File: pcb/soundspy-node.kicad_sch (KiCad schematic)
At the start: 1 part

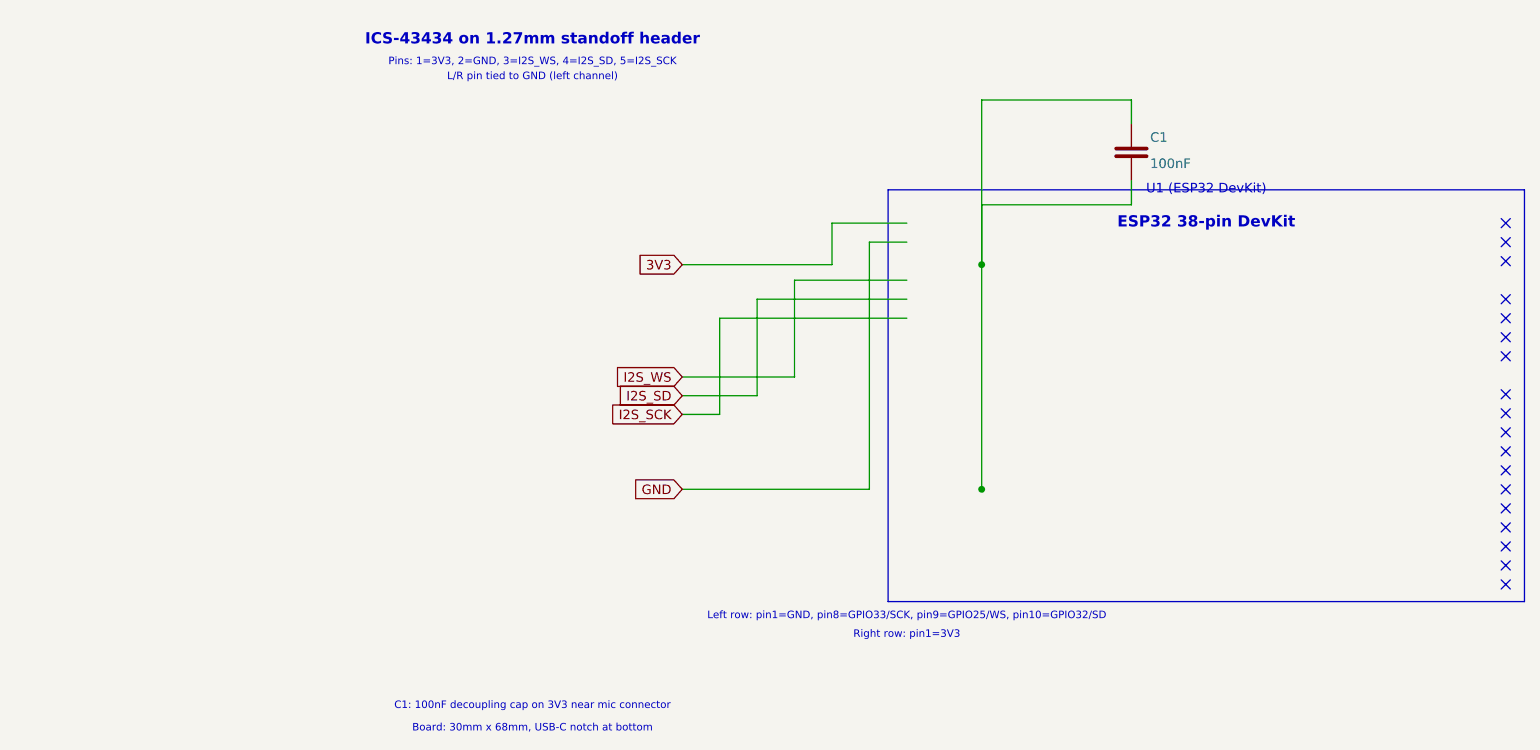
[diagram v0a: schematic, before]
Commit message: Fix PCB and schematic files: remove invalid ;; comments, simplify schematic to valid KiCad syntax
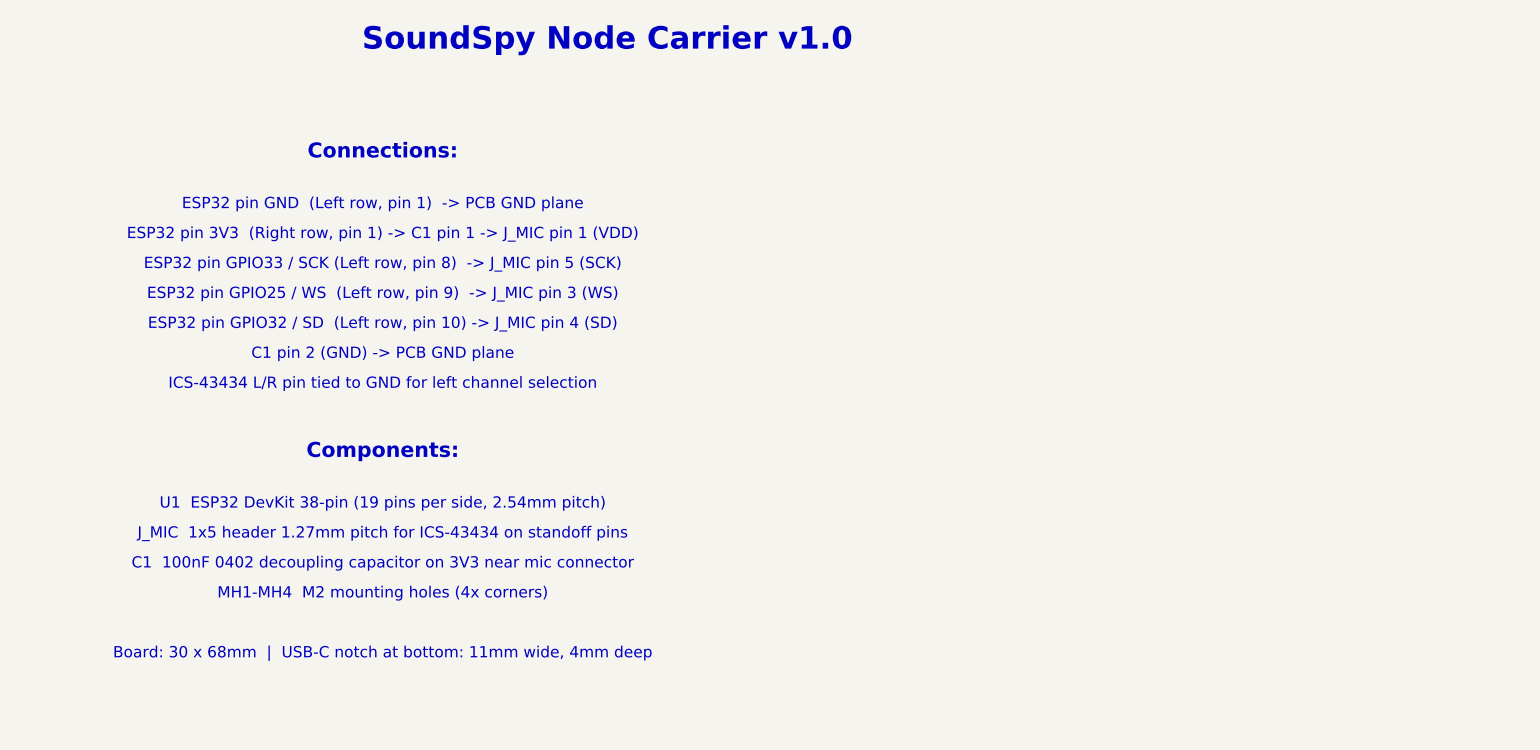
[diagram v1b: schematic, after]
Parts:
- removed C1: 100nF, Capacitor_SMD:C_0402_1005Metric, symbol Device:C
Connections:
- no-connect marks 18 -> 0
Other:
- note added: "Board: 30 x 68mm | USB-C notch at bottom: 11mm wide, 4mm deep"
- note added: "C1 100nF 0402 decoupling capacitor on 3V3 near mic connector"
- note added: "C1 pin 2 (GND) -> PCB GND plane"
- note added: "Components:"
- note added: "Connections:"
- note added: "ESP32 pin 3V3 (Right row, pin 1) -> C1 pin 1 -> J_MIC pin 1 (VDD)"
- note added: "ESP32 pin GND (Left row, pin 1) -> PCB GND plane"
- note added: "ESP32 pin GPIO25 / WS (Left row, pin 9) -> J_MIC pin 3 (WS)"
- note added: "ESP32 pin GPIO32 / SD (Left row, pin 10) -> J_MIC pin 4 (SD)"
- note added: "ESP32 pin GPIO33 / SCK (Left row, pin 8) -> J_MIC pin 5 (SCK)"
- note added: "ICS-43434 L/R pin tied to GND for left channel selection"
- note added: "J_MIC 1x5 header 1.27mm pitch for ICS-43434 on standoff pins"
- note added: "MH1-MH4 M2 mounting holes (4x corners)"
- note added: "SoundSpy Node Carrier v1.0"
- note added: "U1 ESP32 DevKit 38-pin (19 pins per side, 2.54mm pitch)"
- note removed: "Board: 30mm x 68mm, USB-C notch at bottom"
- note removed: "C1: 100nF decoupling cap on 3V3 near mic connector"
- note removed: "ESP32 38-pin DevKit"
- note removed: "ICS-43434 on 1.27mm standoff header"
- note removed: "L/R pin tied to GND (left channel)"
- note removed: "Left row: pin1=GND, pin8=GPIO33/SCK, pin9=GPIO25/WS, pin10=GPIO32/SD"
- note removed: "Pins: 1=3V3, 2=GND, 3=I2S_WS, 4=I2S_SD, 5=I2S_SCK"
- note removed: "Right row: pin1=3V3"
- note removed: "U1 (ESP32 DevKit)"
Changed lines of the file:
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@@
     (rev "1.0")
     (comment 1 "ESP32 38-pin DevKit + ICS-43434 I2S mic carrier")
-    (comment 2 "USB-C notch at bottom for case passthrough")
+    (comment 2 "USB-C notch at bottom edge for case passthrough")
   )
-  (junction (at 100 50) (diameter 0) (color 0 0 0 0))
-  (junction (at 100 80) (diameter 0) (color 0 0 0 0))
-  (no_connect (at 170 44.45) (uuid "nc000001"))
-  (no_connect (at 170 46.99) (uuid "nc000002"))
-  (no_connect (at 170 49.53) (uuid "nc000003"))
-  (no_connect (at 170 54.61) (uuid "nc000004"))
-  (no_connect (at 170 57.15) (uuid "nc000005"))
-  (no_connect (at 170 59.69) (uuid "nc000006"))
-  (no_connect (at 170 62.23) (uuid "nc000007"))
-  (no_connect (at 170 67.31) (uuid "nc000008"))
-  (no_connect (at 170 69.85) (uuid "nc000009"))
-  (no_connect (at 170 72.39) (uuid "nc000010"))
-  (no_connect (at 170 74.93) (uuid "nc000011"))
-  (no_connect (at 170 77.47) (uuid "nc000012"))
-  (no_connect (at 170 80.01) (uuid "nc000013"))
-  (no_connect (at 170 82.55) (uuid "nc000014"))
-  (no_connect (at 170 85.09) (uuid "nc000015"))
-  (no_connect (at 170 87.63) (uuid "nc000016"))
-  (no_connect (at 170 90.17) (uuid "nc000017"))
-  (no_connect (at 170 92.71) (uuid "nc000018"))
-  (wire (pts (xy 90 44.45) (xy 80 44.45)) (stroke (width 0)) (uuid "w000001"))
-  (wire (pts (xy 80 44.45) (xy 80 50)) (stroke (width 0)) (uuid "w000002"))
-  (wire (pts (xy 80 50) (xy 60 50)) (stroke (width 0)) (uuid "w000003"))
-  (wire (pts (xy 90 46.99) (xy 85 46.99)) (stroke (width 0)) (uuid "w000004"))
-  (wire (pts (xy 85 46.99) (xy 85 80)) (stroke (width 0)) (uuid "w000005"))
-  (wire (pts (xy 85 80) (xy 60 80)) (stroke (width 0)) (uuid "w000006"))
-  (wire (pts (xy 90 52.07) (xy 75 52.07)) (stroke (width 0)) (uuid "w000007"))
-  (wire (pts (xy 75 52.07) (xy 75 65)) (stroke (width 0)) (uuid "w000008"))
-  (wire (pts (xy 75 65) (xy 60 65)) (stroke (width 0)) (uuid "w000009"))
-  (wire (pts (xy 90 54.61) (xy 70 54.61)) (stroke (width 0)) (uuid "w000010"))
-  (wire (pts (xy 70 54.61) (xy 70 67.5)) (stroke (width 0)) (uuid "w000011"))
-  (wire (pts (xy 70 67.5) (xy 60 67.5)) (stroke (width 0)) (uuid "w000012"))
-  (wire (pts (xy 90 57.15) (xy 65 57.15)) (stroke (width 0)) (uuid "w000013"))
-  (wire (pts (xy 65 57.15) (xy 65 70)) (stroke (width 0)) (uuid "w000014"))
-  (wire (pts (xy 65 70) (xy 60 70)) (stroke (width 0)) (uuid "w000015"))
-  (global_label "3V3" (shape input) (at 60 50 180)
-    (effects (font (size 1.27 1.27)) (justify right))
-    (uuid "gl000001"))
-  (global_label "GND" (shape input) (at 60 80 180)
-    (effects (font (size 1.27 1.27)) (justify right))
-    (uuid "gl000002"))
-  (global_label "I2S_WS" (shape input) (at 60 65 180)
-    (effects (font (size 1.27 1.27)) (justify right))
-    (uuid "gl000003"))
-  (global_label "I2S_SD" (shape input) (at 60 67.5 180)
-    (effects (font (size 1.27 1.27)) (justify right))
-    (uuid "gl000004"))
-  (global_label "I2S_SCK" (shape input) (at 60 70 180)
-    (effects (font (size 1.27 1.27)) (justify right))
-    (uuid "gl000005"))
-  (symbol (lib_id "Device:C") (at 120 35 0) (unit 1)
-    (property "Reference" "C1" (at 122.5 33 0) (effects (font (size 1.27 1.27)) (justify left)))
-    (property "Value" "100nF" (at 122.5 36.5 0) (effects (font (size 1.27 1.27)) (justify left)))
-    (property "Footprint" "Capacitor_SMD:C_0402_1005Metric" (at 120 35 0) (effects (font (size 1.27 1.27)) (hide)))
-    (pin "1" (uuid "p_c1_1"))
-    (pin "2" (uuid "p_c1_2"))
-  )
-  (wire (pts (xy 120 31.19) (xy 120 28)) (stroke (width 0)) (uuid "w000020"))
-  (wire (pts (xy 120 28) (xy 100 28)) (stroke (width 0)) (uuid "w000021"))
-  (wire (pts (xy 100 28) (xy 100 50)) (stroke (width 0)) (uuid "w000022"))
-  (wire (pts (xy 120 38.81) (xy 120 42)) (stroke (width 0)) (uuid "w000023"))
-  (wire (pts (xy 120 42) (xy 100 42)) (stroke (width 0)) (uuid "w000024"))
-  (wire (pts (xy 100 42) (xy 100 80)) (stroke (width 0)) (uuid "w000025"))
-  (text "ESP32 38-pin DevKit" (at 130 44.45 0) (effects (font (size 1.5 1.5) (bold yes))))
-  (text "Left row: pin1=GND, pin8=GPIO33/SCK, pin9=GPIO25/WS, pin10=GPIO32/SD" (at 90 97 0) (effects (font (size 1.0 1.0))))
-  (text "Right row: pin1=3V3" (at 90 99.5 0) (effects (font (size 1.0 1.0))))
-  (text "ICS-43434 on 1.27mm standoff header" (at 40 20 0) (effects (font (size 1.5 1.5) (bold yes))))
-  (text "Pins: 1=3V3, 2=GND, 3=I2S_WS, 4=I2S_SD, 5=I2S_SCK" (at 40 23 0) (effects (font (size 1.0 1.0))))
-  (text "L/R pin tied to GND (left channel)" (at 40 25 0) (effects (font (size 1.0 1.0))))
-  (text "C1: 100nF decoupling cap on 3V3 near mic connector" (at 40 109 0) (effects (font (size 1.0 1.0))))
-  (text "Board: 30mm x 68mm, USB-C notch at bottom" (at 40 112 0) (effects (font (size 1.0 1.0))))
-  (rectangle (start 87.5 40) (end 172.5 95)
-    (stroke (width 0.15)) (fill (type none)) (uuid "rect000001"))
-  (text "U1 (ESP32 DevKit)" (at 130 40 0) (effects (font (size 1.27 1.27))))
-  (pin_list
-    (pin (number "1") (name "GND") (at 90 44.45 0) (uuid "esp_l1"))
-    (pin (number "8") (name "GPIO33/SCK") (at 90 52.07 0) (uuid "esp_l8"))
-    (pin (number "9") (name "GPIO25/WS") (at 90 54.61 0) (uuid "esp_l9"))
-    (pin (number "10") (name "GPIO32/SD") (at 90 57.15 0) (uuid "esp_l10"))
-    (pin (number "R1") (name "3V3") (at 170 44.45 0) (uuid "esp_r1"))
-  )
+  (text "SoundSpy Node Carrier v1.0" (at 50 20 0)
+    (effects (font (size 3 3) (bold yes))))
+  (text "Connections:" (at 20 35 0)
+    (effects (font (size 2 2) (bold yes))))
+  (text "ESP32 pin GND  (Left row, pin 1)  -> PCB GND plane" (at 20 42 0)
+    (effects (font (size 1.5 1.5))))
+  (text "ESP32 pin 3V3  (Right row, pin 1) -> C1 pin 1 -> J_MIC pin 1 (VDD)" (at 20 46 0)
+    (effects (font (size 1.5 1.5))))
+  (text "ESP32 pin GPIO33 / SCK (Left row, pin 8)  -> J_MIC pin 5 (SCK)" (at 20 50 0)
+    (effects (font (size 1.5 1.5))))
+  (text "ESP32 pin GPIO25 / WS  (Left row, pin 9)  -> J_MIC pin 3 (WS)" (at 20 54 0)
+    (effects (font (size 1.5 1.5))))
+  (text "ESP32 pin GPIO32 / SD  (Left row, pin 10) -> J_MIC pin 4 (SD)" (at 20 58 0)
+    (effects (font (size 1.5 1.5))))
+  (text "C1 pin 2 (GND) -> PCB GND plane" (at 20 62 0)
+    (effects (font (size 1.5 1.5))))
+  (text "ICS-43434 L/R pin tied to GND for left channel selection" (at 20 66 0)
+    (effects (font (size 1.5 1.5))))
+  (text "Components:" (at 20 75 0)
+    (effects (font (size 2 2) (bold yes))))
+  (text "U1  ESP32 DevKit 38-pin (19 pins per side, 2.54mm pitch)" (at 20 82 0)
+    (effects (font (size 1.5 1.5))))
+  (text "J_MIC  1x5 header 1.27mm pitch for ICS-43434 on standoff pins" (at 20 86 0)
+    (effects (font (size 1.5 1.5))))
+  (text "C1  100nF 0402 decoupling capacitor on 3V3 near mic connector" (at 20 90 0)
+    (effects (font (size 1.5 1.5))))
+  (text "MH1-MH4  M2 mounting holes (4x corners)" (at 20 94 0)
+    (effects (font (size 1.5 1.5))))
+  (text "Board: 30 x 68mm  |  USB-C notch at bottom: 11mm wide, 4mm deep" (at 20 102 0)
+    (effects (font (size 1.5 1.5))))
 )
